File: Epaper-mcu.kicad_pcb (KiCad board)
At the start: 2 copper layers, 85 x 37 mm, 47 parts, among them J1 USB_C_Receptacle_USB2.0, J2 Conn_01x08_Male, Q1 S8050, Q2 S8050, Q3 SI1308EDL-T1-GE3, SW1 SW_Push, SW2 SW_Push, U1 ESP32-WROOM-E, U2 CH340C, U3 AMS1117-3.3

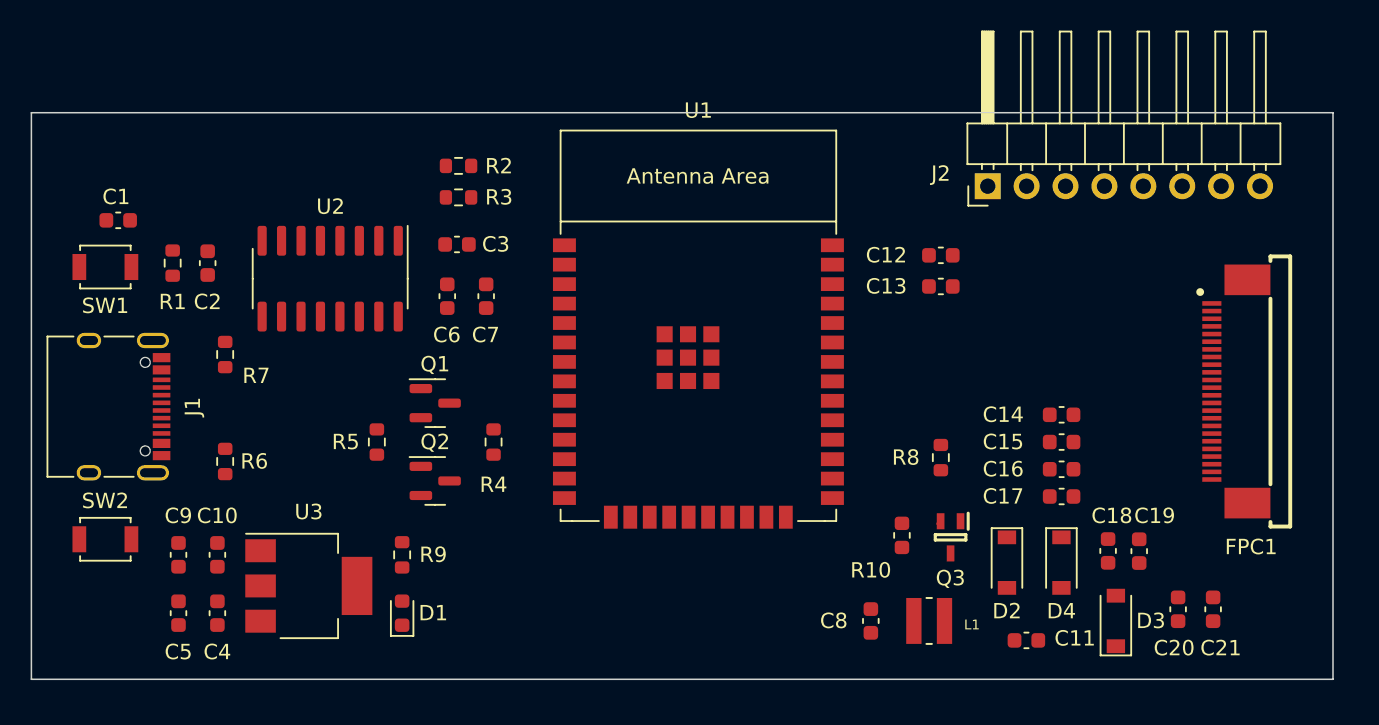
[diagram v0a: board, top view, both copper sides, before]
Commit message: Epaper setup
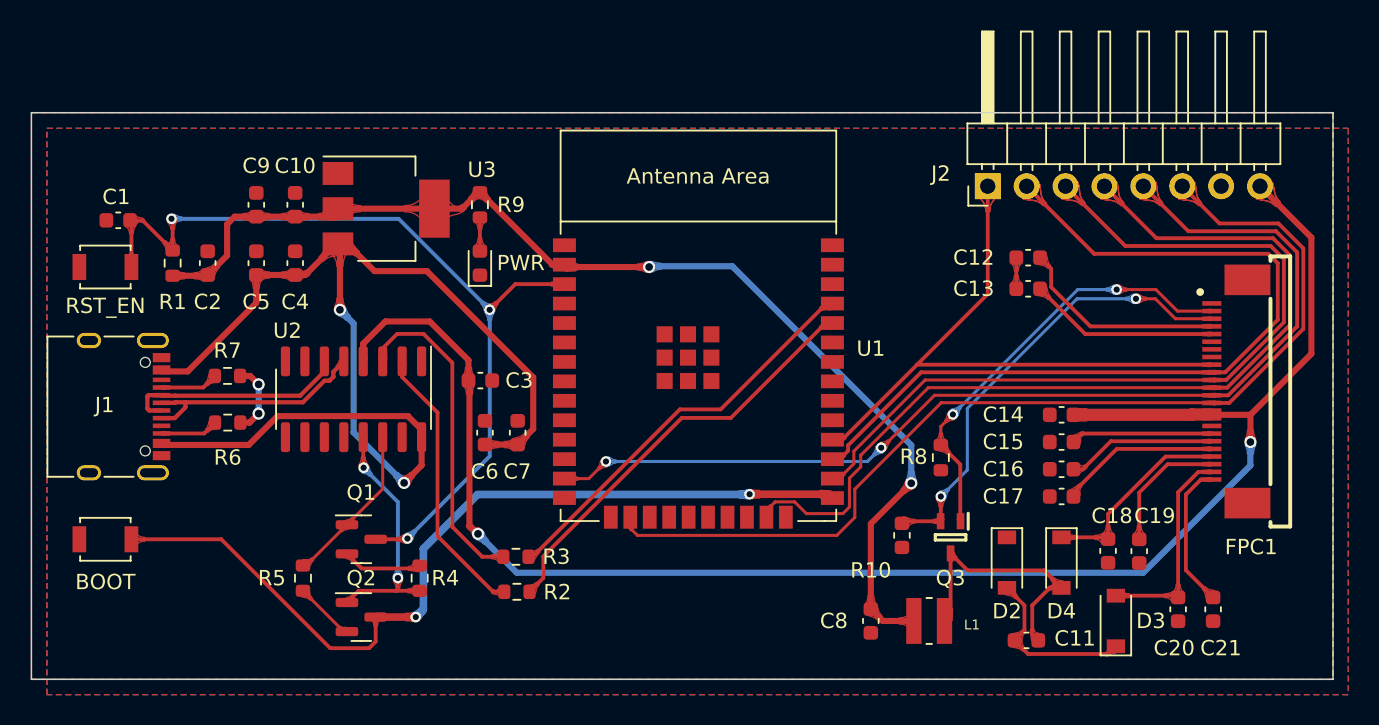
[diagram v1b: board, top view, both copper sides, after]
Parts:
- moved R2 28.1 mm to (142.5, 113.9)
- moved U3 25.2 mm to (134.0, 88.9)
- moved R3 23.8 mm to (142.4, 111.6)
- moved C5 23.4 mm to (125.5, 92.5)
- moved C9 23.4 mm to (125.5, 88.6)
- moved C10 23.4 mm to (128.0, 88.6)
- moved C4 23.4 mm to (128.0, 92.5)
- moved PWR 23.4 mm to (140.1, 92.5)
- moved R9 23.4 mm to (140.1, 88.6)
- moved Q1 10.1 mm to (132.3, 110.5)
- moved R4 10.1 mm to (136.1, 113.0)
- moved R5 10.1 mm to (128.5, 113.0)
- moved Q2 10.1 mm to (132.3, 115.6)
- moved C6 9.25 mm to (140.4, 103.5)
- moved C7 9.15 mm to (142.5, 103.5)
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- renumbered SW2 to BOOT, D1 to PWR, SW1 to RST_EN
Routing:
- net /3V3: track 0.00 -> 108.4 mm, vias 0 -> 2
- net +5V: track 0.00 -> 78.8 mm, vias 0 -> 2
- net +3.3V: track 0.00 -> 73.5 mm, vias 0 -> 2
- net /CLK: track 0.00 -> 68.6 mm, vias 0 -> 2
- net /SDA: track 0.00 -> 66.4 mm
- net /CS: track 0.00 -> 60.4 mm
- net /RST_EN: track 0.00 -> 56.9 mm, vias 0 -> 3
- net /BOOT: track 0.00 -> 56.3 mm, vias 0 -> 2
- net /RST: track 0.00 -> 55.2 mm
- net /DC: track 0.00 -> 54.5 mm
- net /BUSY: track 0.00 -> 40.4 mm
- net /RESE: track 0.23 -> 30.1 mm, vias 0 -> 2
- net /GDR: track 0.00 -> 28.7 mm, vias 0 -> 2
- net Net-(R2-Pad2): track 0.00 -> 27.9 mm
- net Net-(R3-Pad2): track 0.00 -> 27.3 mm
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- added copper zone on B.Cu, net GND
- added copper zone on F.Cu, net GND
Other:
- board text added: "3V3"
- board text added: "BUSY"
- board text added: "CLK"
- board text added: "CS"
- board text added: "DC"
- board text added: "GND"
- board text added: "RST"
- board text added: "SDA"
